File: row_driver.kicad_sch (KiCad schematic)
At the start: 26 parts, among them SW3 SW_PUSH_SMALL_H, SW4 SW_PUSH_SMALL_H, SW5 SW_PUSH_SMALL_H, SW6 SW_PUSH_SMALL_H, SW7 SW_PUSH_SMALL_H, SW8 SW_PUSH_SMALL_H, U11 74HCT595, U13 74HCT595, U15 74HCT595, U23 CM1293A-04SO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

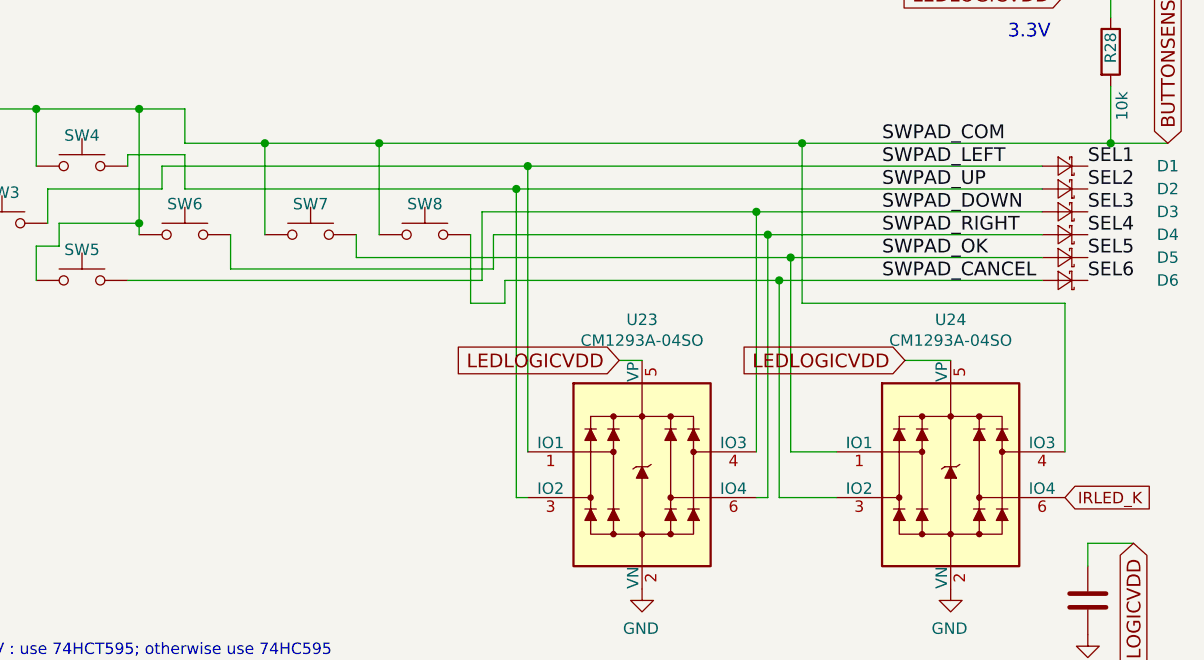
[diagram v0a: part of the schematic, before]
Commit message: Button component change and removed some ESD diodes
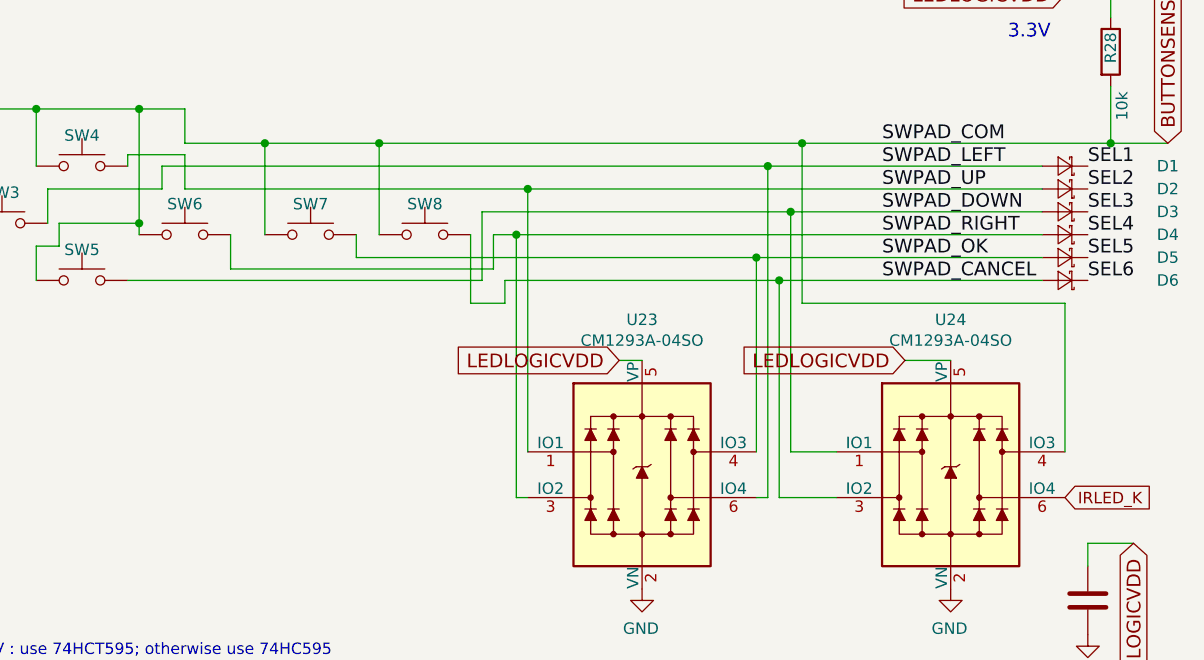
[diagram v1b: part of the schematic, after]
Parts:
- SW3, SW4, SW5, SW6, SW7, SW8: footprint components:TACT_SW_SMD_Panasonic-EVPAWBD2A -> Button_Switch_THT:SW_PUSH_6mm_H5mm
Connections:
- net SWPAD_DOWN: now also U24.1 (IO1); no longer U23.4 (IO3)
- net SWPAD_LEFT: now also U23.6 (IO4); no longer U23.1 (IO1)
- net SWPAD_OK: now also U23.4 (IO3); no longer U24.1 (IO1)
- net SWPAD_RIGHT: now also U23.3 (IO2); no longer U23.6 (IO4)
- net SWPAD_UP: now also U23.1 (IO1); no longer U23.3 (IO2)
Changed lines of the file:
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@@
 (kicad_sch (version 20200608) (host eeschema "5.99.0-unknown-60915fb~88~ubuntu18.04.1")
-  (page 5 10)
+  (page 4 10)
   (paper "A4")
   (junction (at 43.18 147.32))
@@
   (junction (at 177.8 41.91))
   (junction (at 190.5 41.91))
-  (junction (at 205.74 46.99))
-  (junction (at 207.01 44.45))
-  (junction (at 232.41 49.53))
-  (junction (at 233.68 52.07))
+  (junction (at 205.74 52.07))
+  (junction (at 207.01 46.99))
+  (junction (at 232.41 54.61))
+  (junction (at 233.68 44.45))
   (junction (at 234.95 57.15))
-  (junction (at 236.22 54.61))
+  (junction (at 236.22 49.53))
   (junction (at 237.49 41.91))
   (junction (at 241.3 128.27))
@@
     (stroke (width 0) (type solid) (color 0 0 0 0))
   )
-  (wire (pts (xy 166.37 44.45) (xy 207.01 44.45))
+  (wire (pts (xy 166.37 44.45) (xy 233.68 44.45))
     (stroke (width 0) (type solid) (color 0 0 0 0))
   )
@@
     (stroke (width 0) (type solid) (color 0 0 0 0))
   )
-  (wire (pts (xy 168.91 46.99) (xy 205.74 46.99))
+  (wire (pts (xy 168.91 46.99) (xy 207.01 46.99))
     (stroke (width 0) (type solid) (color 0 0 0 0))
   )
@@
     (stroke (width 0) (type solid) (color 0 0 0 0))
   )
-  (wire (pts (xy 187.96 54.61) (xy 236.22 54.61))
+  (wire (pts (xy 187.96 54.61) (xy 232.41 54.61))
     (stroke (width 0) (type solid) (color 0 0 0 0))
   )
@@
     (stroke (width 0) (type solid) (color 0 0 0 0))
   )
-  (wire (pts (xy 201.93 49.53) (xy 232.41 49.53))
+  (wire (pts (xy 201.93 49.53) (xy 236.22 49.53))
     (stroke (width 0) (type solid) (color 0 0 0 0))
   )
@@
     (stroke (width 0) (type solid) (color 0 0 0 0))
   )
-  (wire (pts (xy 203.2 52.07) (xy 233.68 52.07))
+  (wire (pts (xy 203.2 52.07) (xy 205.74 52.07))
     (stroke (width 0) (type solid) (color 0 0 0 0))
   )
@@
     (stroke (width 0) (type solid) (color 0 0 0 0))
   )
-  (wire (pts (xy 205.74 46.99) (xy 264.16 46.99))
-    (stroke (width 0) (type solid) (color 0 0 0 0))
-  )
-  (wire (pts (xy 205.74 81.28) (xy 205.74 46.99))
-    (stroke (width 0) (type solid) (color 0 0 0 0))
-  )
-  (wire (pts (xy 207.01 44.45) (xy 264.16 44.45))
-    (stroke (width 0) (type solid) (color 0 0 0 0))
-  )
-  (wire (pts (xy 207.01 76.2) (xy 207.01 44.45))
+  (wire (pts (xy 205.74 52.07) (xy 205.74 81.28))
+    (stroke (width 0) (type solid) (color 0 0 0 0))
+  )
+  (wire (pts (xy 205.74 52.07) (xy 264.16 52.07))
+    (stroke (width 0) (type solid) (color 0 0 0 0))
+  )
+  (wire (pts (xy 207.01 46.99) (xy 207.01 76.2))
+    (stroke (width 0) (type solid) (color 0 0 0 0))
+  )
+  (wire (pts (xy 207.01 46.99) (xy 264.16 46.99))
     (stroke (width 0) (type solid) (color 0 0 0 0))
   )
@@
     (stroke (width 0) (type solid) (color 0 0 0 0))
   )
-  (wire (pts (xy 232.41 49.53) (xy 264.16 49.53))
-    (stroke (width 0) (type solid) (color 0 0 0 0))
-  )
-  (wire (pts (xy 232.41 76.2) (xy 232.41 49.53))
+  (wire (pts (xy 232.41 54.61) (xy 232.41 76.2))
+    (stroke (width 0) (type solid) (color 0 0 0 0))
+  )
+  (wire (pts (xy 232.41 54.61) (xy 264.16 54.61))
     (stroke (width 0) (type solid) (color 0 0 0 0))
   )
@@
     (stroke (width 0) (type solid) (color 0 0 0 0))
   )
-  (wire (pts (xy 233.68 52.07) (xy 264.16 52.07))
-    (stroke (width 0) (type solid) (color 0 0 0 0))
-  )
-  (wire (pts (xy 233.68 81.28) (xy 233.68 52.07))
+  (wire (pts (xy 233.68 44.45) (xy 233.68 81.28))
+    (stroke (width 0) (type solid) (color 0 0 0 0))
+  )
+  (wire (pts (xy 233.68 44.45) (xy 264.16 44.45))
+    (stroke (width 0) (type solid) (color 0 0 0 0))
+  )
+  (wire (pts (xy 234.95 57.15) (xy 234.95 81.28))
     (stroke (width 0) (type solid) (color 0 0 0 0))
   )
@@
     (stroke (width 0) (type solid) (color 0 0 0 0))
   )
-  (wire (pts (xy 234.95 81.28) (xy 234.95 57.15))
-    (stroke (width 0) (type solid) (color 0 0 0 0))
-  )
-  (wire (pts (xy 236.22 54.61) (xy 264.16 54.61))
-    (stroke (width 0) (type solid) (color 0 0 0 0))
-  )
-  (wire (pts (xy 236.22 76.2) (xy 236.22 54.61))
+  (wire (pts (xy 236.22 49.53) (xy 236.22 76.2))
+    (stroke (width 0) (type solid) (color 0 0 0 0))
+  )
+  (wire (pts (xy 236.22 49.53) (xy 264.16 49.53))
     (stroke (width 0) (type solid) (color 0 0 0 0))
   )
@@
     (property "Datasheet" "" (id 3) (at 137.16 45.72 0))
   )
-  (symbol (lib_id "dotmatrix_64x48-rescue:R-device") (at 232.41 128.27 270) (mirror x)
+  (symbol (lib_id "dotmatrix_64x48-rescue:R-device") (at 232.41 128.27 270) (mirror x) (unit 1)
     (in_bom yes) (on_board yes)
     (property "Reference" "R119" (id 0) (at 229.87 128.27 90)
@@
     (property "Datasheet" "" (id 3) (at 232.41 128.27 0))
   )
-  (symbol (lib_id "dotmatrix_64x48-rescue:R-device") (at 241.3 135.89 0) (mirror y)
+  (symbol (lib_id "dotmatrix_64x48-rescue:R-device") (at 241.3 135.89 0) (mirror y) (unit 1)
     (in_bom yes) (on_board yes)
     (property "Reference" "R46" (id 0) (at 241.3 138.43 90)
@@
       (effects (font (size 1.27 1.27)) hide)
     )
-    (property "Footprint" "components:TACT_SW_SMD_Panasonic-EVPAWBD2A" (id 2) (at 148.59 45.72 0)
+    (property "Footprint" "Button_Switch_THT:SW_PUSH_6mm_H5mm" (id 2) (at 148.59 45.72 0)
       (effects (font (size 1.27 1.27)) hide)
     )
@@
       (effects (font (size 1.27 1.27)) hide)
     )
-    (property "Footprint" "components:TACT_SW_SMD_Panasonic-EVPAWBD2A" (id 2) (at 157.48 39.37 0)
+    (property "Footprint" "Button_Switch_THT:SW_PUSH_6mm_H5mm" (id 2) (at 157.48 39.37 0)
       (effects (font (size 1.27 1.27)) hide)
     )
@@
       (effects (font (size 1.27 1.27)) hide)
     )
-    (property "Footprint" "components:TACT_SW_SMD_Panasonic-EVPAWBD2A" (id 2) (at 157.48 52.07 0)
+    (property "Footprint" "Button_Switch_THT:SW_PUSH_6mm_H5mm" (id 2) (at 157.48 52.07 0)
       (effects (font (size 1.27 1.27)) hide)
     )
@@
       (effects (font (size 1.27 1.27)) hide)
     )
-    (property "Footprint" "components:TACT_SW_SMD_Panasonic-EVPAWBD2A" (id 2) (at 168.91 46.99 0)
+    (property "Footprint" "Button_Switch_THT:SW_PUSH_6mm_H5mm" (id 2) (at 168.91 46.99 0)
       (effects (font (size 1.27 1.27)) hide)
     )
@@
       (effects (font (size 1.27 1.27)) hide)
     )
-    (property "Footprint" "components:TACT_SW_SMD_Panasonic-EVPAWBD2A" (id 2) (at 182.88 46.99 0)
+    (property "Footprint" "Button_Switch_THT:SW_PUSH_6mm_H5mm" (id 2) (at 182.88 46.99 0)
       (effects (font (size 1.27 1.27)) hide)
     )
@@
       (effects (font (size 1.27 1.27)) hide)
     )
-    (property "Footprint" "components:TACT_SW_SMD_Panasonic-EVPAWBD2A" (id 2) (at 195.58 46.99 0)
+    (property "Footprint" "Button_Switch_THT:SW_PUSH_6mm_H5mm" (id 2) (at 195.58 46.99 0)
       (effects (font (size 1.27 1.27)) hide)
     )
@@
   )
   (sheet (at 36.83 40.64) (size 20.32 17.78)
-    (stroke (width 0) (type solid) (color 0 0 0 0))
-    (fill (color 0 0 0 0.0000))
+    (stroke (width 0) (type solid) (color 132 0 132 1))
+    (fill (color 255 255 255 0.0000))
     (property "Sheet name" "f_r0" (id 0) (at 36.0675 58.42 90)
       (effects (font (size 1.524 1.524)) (justify left bottom))
@@
   )
   (sheet (at 105.41 40.64) (size 20.32 17.78)
-    (stroke (width 0) (type solid) (color 0 0 0 0))
-    (fill (color 0 0 0 0.0000))
+    (stroke (width 0) (type solid) (color 132 0 132 1))
+    (fill (color 255 255 255 0.0000))
     (property "Sheet name" "f_r16" (id 0) (at 104.6475 58.42 90)
       (effects (font (size 1.524 1.524)) (justify left bottom))
@@
   )
   (sheet (at 71.12 40.64) (size 20.32 17.78)
-    (stroke (width 0) (type solid) (color 0 0 0 0))
-    (fill (color 0 0 0 0.0000))
+    (stroke (width 0) (type solid) (color 132 0 132 1))
+    (fill (color 255 255 255 0.0000))
     (property "Sheet name" "f_r8" (id 0) (at 70.3575 58.42 90)
       (effects (font (size 1.524 1.524)) (justify left bottom))

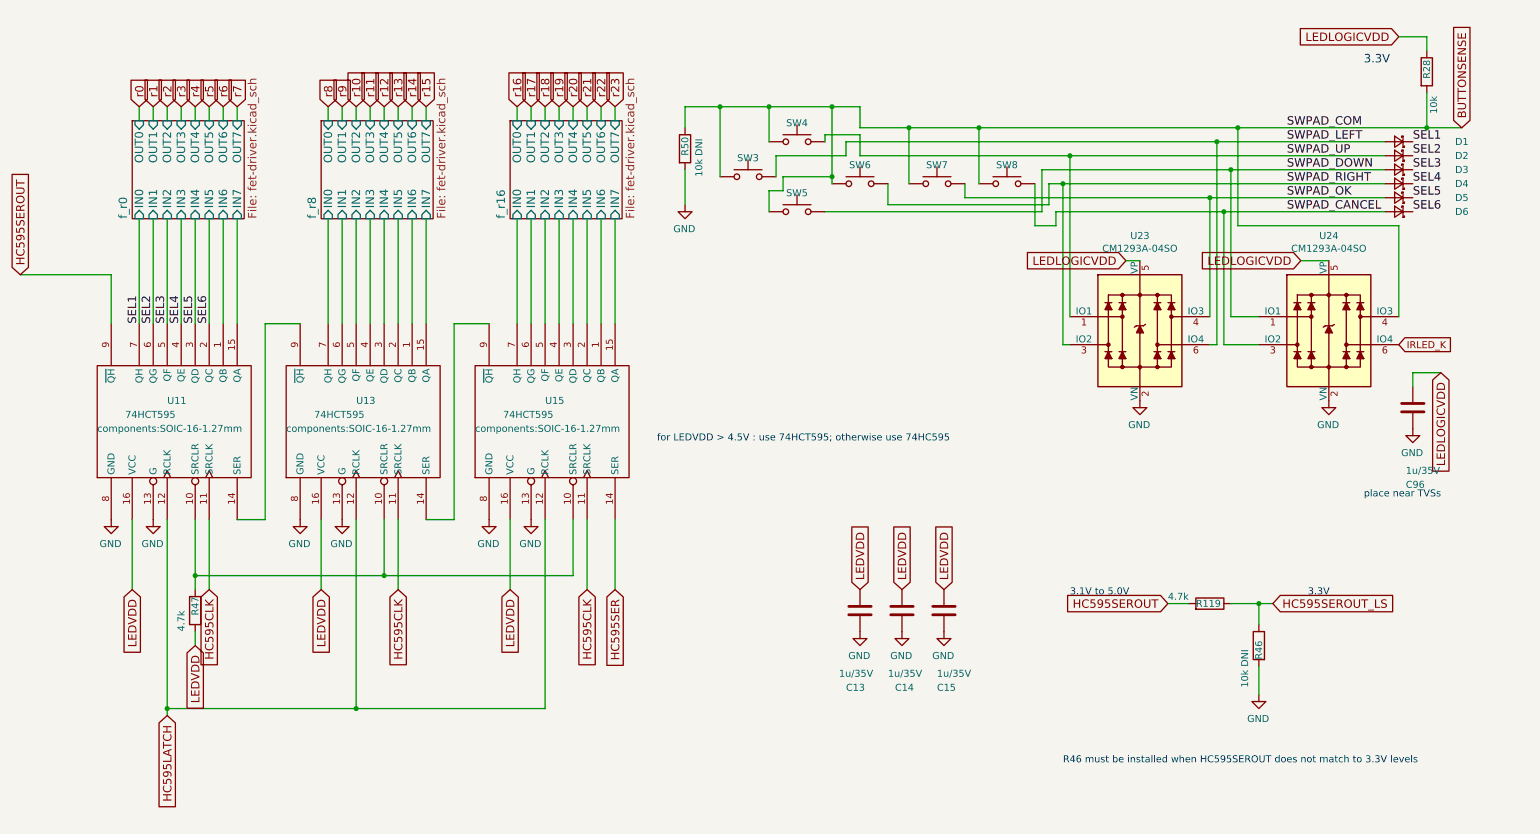
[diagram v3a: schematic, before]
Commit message: WROOM32 coupling capacitor order fixed; Added FB on long line to board left-most sensors
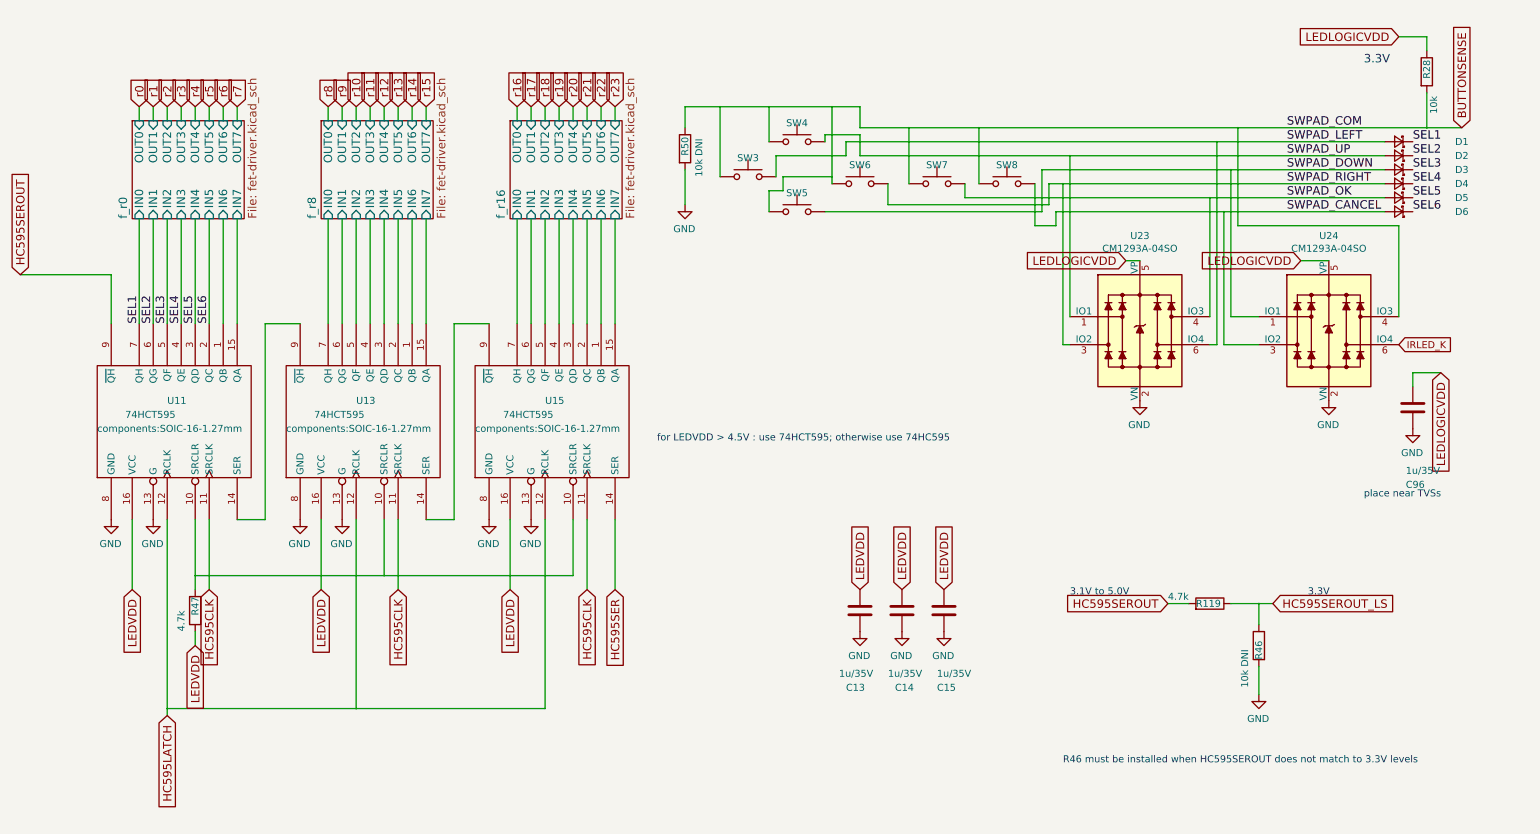
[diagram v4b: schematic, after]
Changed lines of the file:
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@@
-(kicad_sch (version 20200618) (host eeschema "5.99.0-unknown-7340c97~89~ubuntu18.04.1")
-  (page 1 10)
+(kicad_sch (version 20200714) (host eeschema "5.99.0-unknown-e5f2015a9~89~ubuntu18.04.1")
+  (page 4 10)
   (paper "A4")
-  (junction (at 43.18 147.32) (diameter 0) (color 0 0 0 0))
-  (junction (at 48.26 123.19) (diameter 0) (color 0 0 0 0))
-  (junction (at 77.47 147.32) (diameter 0) (color 0 0 0 0))
-  (junction (at 82.55 123.19) (diameter 0) (color 0 0 0 0))
-  (junction (at 143.51 38.1) (diameter 0) (color 0 0 0 0))
-  (junction (at 152.4 38.1) (diameter 0) (color 0 0 0 0))
-  (junction (at 163.83 38.1) (diameter 0) (color 0 0 0 0))
-  (junction (at 163.83 50.8) (diameter 0) (color 0 0 0 0))
-  (junction (at 177.8 41.91) (diameter 0) (color 0 0 0 0))
-  (junction (at 190.5 41.91) (diameter 0) (color 0 0 0 0))
-  (junction (at 205.74 52.07) (diameter 0) (color 0 0 0 0))
-  (junction (at 207.01 46.99) (diameter 0) (color 0 0 0 0))
-  (junction (at 232.41 54.61) (diameter 0) (color 0 0 0 0))
-  (junction (at 233.68 44.45) (diameter 0) (color 0 0 0 0))
-  (junction (at 234.95 57.15) (diameter 0) (color 0 0 0 0))
-  (junction (at 236.22 49.53) (diameter 0) (color 0 0 0 0))
-  (junction (at 237.49 41.91) (diameter 0) (color 0 0 0 0))
-  (junction (at 241.3 128.27) (diameter 0) (color 0 0 0 0))
-  (junction (at 271.78 41.91) (diameter 0) (color 0 0 0 0))
+  (junction (at 43.18 147.32) (diameter 0.3048) (color 0 0 0 0))
+  (junction (at 48.26 123.19) (diameter 0.3048) (color 0 0 0 0))
+  (junction (at 77.47 147.32) (diameter 0.3048) (color 0 0 0 0))
+  (junction (at 82.55 123.19) (diameter 0.3048) (color 0 0 0 0))
+  (junction (at 143.51 38.1) (diameter 0.3048) (color 0 0 0 0))
+  (junction (at 152.4 38.1) (diameter 0.3048) (color 0 0 0 0))
+  (junction (at 163.83 38.1) (diameter 0.3048) (color 0 0 0 0))
+  (junction (at 163.83 50.8) (diameter 0.3048) (color 0 0 0 0))
+  (junction (at 177.8 41.91) (diameter 0.3048) (color 0 0 0 0))
+  (junction (at 190.5 41.91) (diameter 0.3048) (color 0 0 0 0))
+  (junction (at 205.74 52.07) (diameter 0.3048) (color 0 0 0 0))
+  (junction (at 207.01 46.99) (diameter 0.3048) (color 0 0 0 0))
+  (junction (at 232.41 54.61) (diameter 0.3048) (color 0 0 0 0))
+  (junction (at 233.68 44.45) (diameter 0.3048) (color 0 0 0 0))
+  (junction (at 234.95 57.15) (diameter 0.3048) (color 0 0 0 0))
+  (junction (at 236.22 49.53) (diameter 0.3048) (color 0 0 0 0))
+  (junction (at 237.49 41.91) (diameter 0.3048) (color 0 0 0 0))
+  (junction (at 241.3 128.27) (diameter 0.3048) (color 0 0 0 0))
+  (junction (at 271.78 41.91) (diameter 0.3048) (color 0 0 0 0))
   (wire (pts (xy 16.51 68.58) (xy 33.02 68.58))
     (stroke (width 0) (type solid) (color 0 0 0 0))
